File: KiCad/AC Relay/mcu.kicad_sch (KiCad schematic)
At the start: 37 parts, among them J10 Conn_ARM_SWD_TagConnect_TC203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, J4 Conn_01x06_Female, J5 Boot, J6 TB002-500-02BE, J7 TB002-500-02BE, J8 TB002-500-02BE, J9 Conn_ARM_SWD_TagConnect_TC2030, SW1 SW_Push, SW2 Boot, SW3 Rst, U3 ESP-12E, U4 ESP32-WROOM-32UE

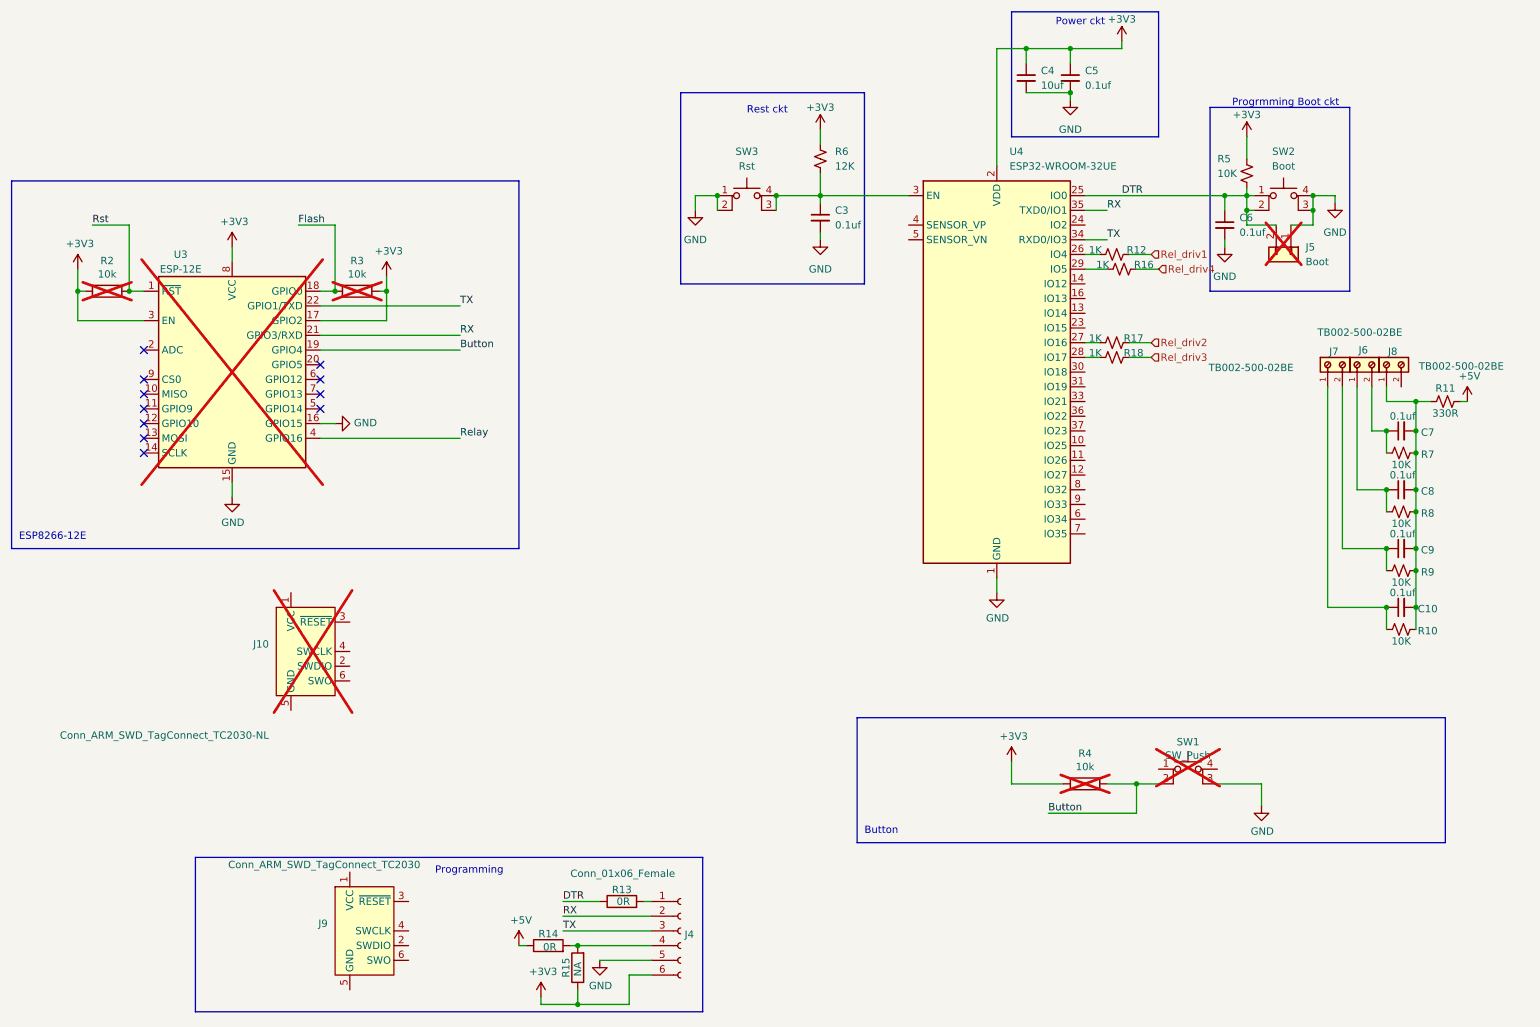
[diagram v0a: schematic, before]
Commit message: error elemination
schametic error elemination
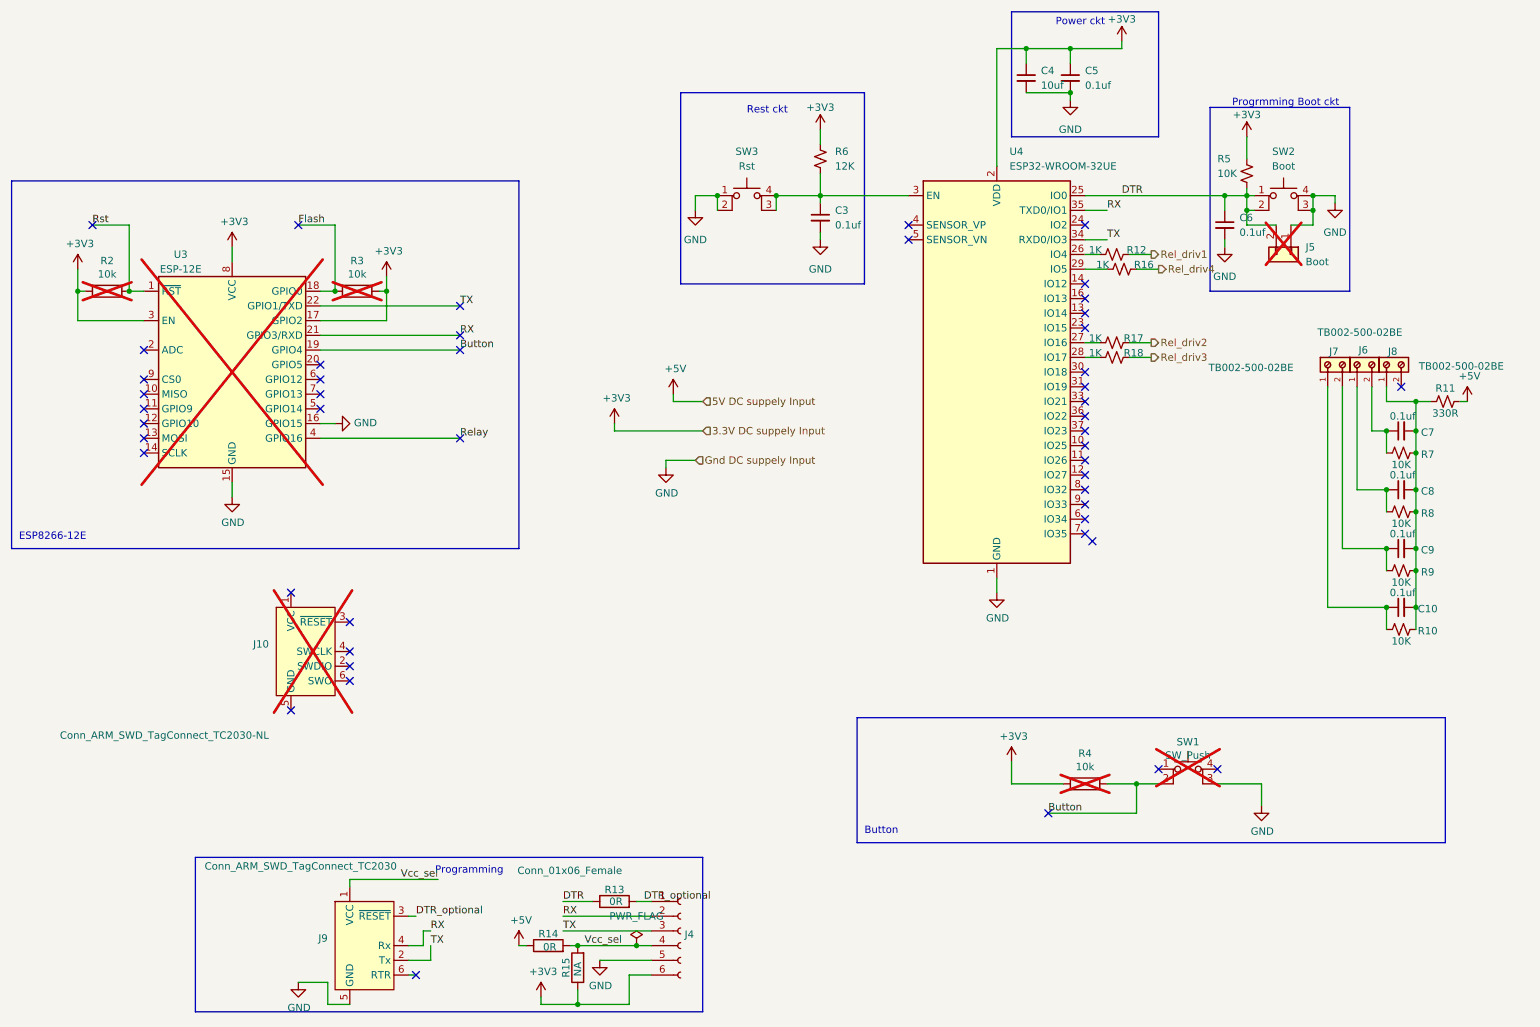
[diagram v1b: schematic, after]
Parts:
- J9: symbol Connector:Conn_ARM_SWD_TagConnect_TC2030 -> Rak_sym_Libr:Conn_Esp_TagConnect_TC2030_1_
- U4: footprint Rak_FP_Library:ESP32-WROOM-32UE -> RF_Module:ESP32-WROOM-32UE
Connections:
- net GND: now also J9.5 (GND)
- net RX: now also J9.4 (Rx)
- net TX: now also J9.2 (Tx)
- net Vcc_sel: now reaches J4.4 (Pin_4), R14.2, R15.2
- net Vcc_sel: now also J9.1 (VCC)
- net DTR_optional: now reaches J4.1 (Pin_1), R13.2
- net DTR_optional: now also J9.3 (~{RESET})
- no-connect marks 11 -> 48
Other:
- moved on the sheet: J9, R13
